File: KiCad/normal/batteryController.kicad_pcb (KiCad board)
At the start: 2 copper layers, 52.5 x 35 mm, 20 parts, among them J1 Screw_Terminal_01x02, J2 Conn_01x04_Male, J3 Conn_01x04_Male, J4 Conn_01x04_Male, J5 Conn_02x04_Odd_Even, J6 Conn_01x01_Male, J7 USB_A, U1 ATtiny45V-10P, U2 LM2596S-ADJ, U3 LP2950-3.3_TO92

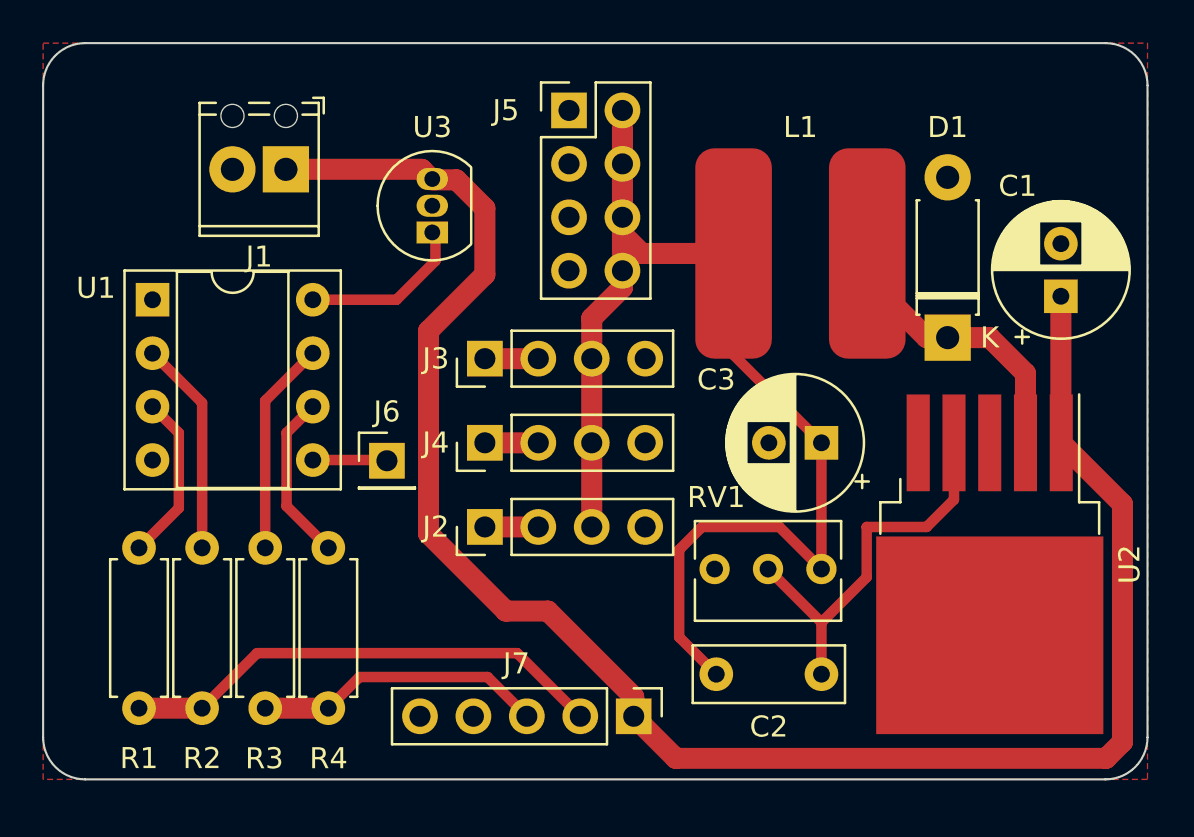
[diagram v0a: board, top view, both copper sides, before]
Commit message: made version using smt components
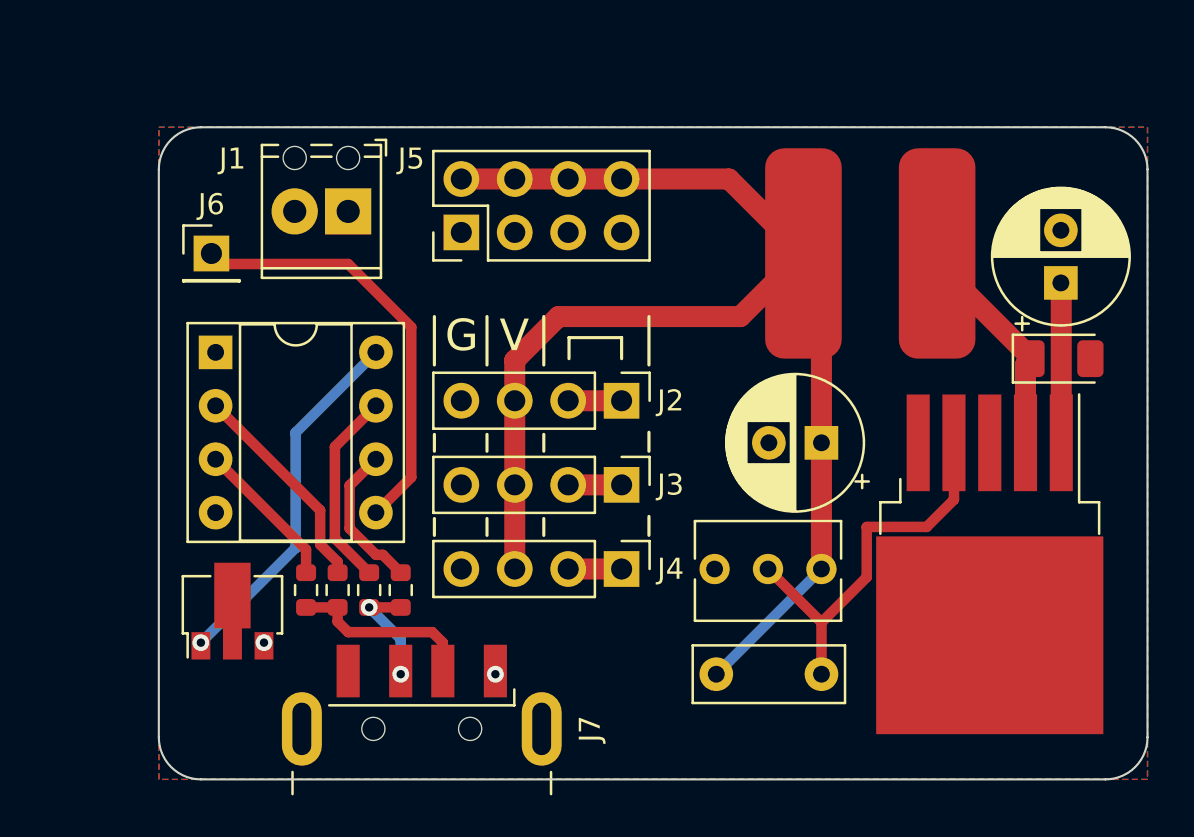
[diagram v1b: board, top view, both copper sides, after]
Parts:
- D1: footprint Diode_THT:D_DO-41_SOD81_P7.62mm_Horizontal -> Diode_SMD:D_1206_3216Metric
- J7: footprint Connector_PinHeader_2.54mm:PinHeader_1x05_P2.54mm_Vertical -> Connector_USB:USB_A_CNCTech_1001-011-01101_Horizontal
- R1, R2, R3, R4: footprint Resistor_THT:R_Axial_DIN0207_L6.3mm_D2.5mm_P7.62mm_Horizontal -> Resistor_SMD:R_0603_1608Metric
- U3: footprint Package_TO_SOT_THT:TO-92_Inline -> Package_TO_SOT_SMD:SOT-89-3
- moved U3 20.4 mm to (57.0, 78.0)
- moved J6 12.9 mm to (56.0, 61.0)
- moved J7 12.6 mm to (66.0, 90.5)
- moved J2 8.85 mm to (75.5, 68.0), turned to -90 degrees
- moved J3 8.85 mm to (75.5, 72.0), turned to -90 degrees
- moved J4 8.85 mm to (75.5, 76.0), turned to -90 degrees
- moved R1 8.19 mm to (60.5, 77.0)
- moved J5 7.74 mm to (67.9, 60.0), turned to 90 degrees
- moved R2 6.75 mm to (62.0, 77.0)
- moved D1 5.48 mm to (96.4, 66.0), turned to 0 degrees
- moved R3 5.33 mm to (63.5, 77.0)
- moved R4 3.98 mm to (65.0, 77.0)
- moved U1 3.91 mm to (56.2, 65.7)
- moved J1 3.57 mm to (62.5, 59.0)
- moved L1 3.32 mm to (87.3, 61.0)
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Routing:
- net /VBUS: track 86.6 -> 7.63 mm, vias 0 -> 2
- net /controll pin: track 3.49 -> 20.5 mm
- net Net-(J7-Pad2): track 23.3 -> 8.94 mm
- net /5V: track 7.45 -> 17.2 mm, vias 0 -> 1
- net /OUT: track 56.7 -> 65.9 mm
- net Net-(J7-Pad3): track 13.8 -> 5.30 mm, vias 0 -> 2
- net /ROUT: track 14.7 -> 11.0 mm
- net Net-(R4-Pad1): track 8.06 -> 7.11 mm
- net Net-(R1-Pad1): track 8.02 -> 7.18 mm
- net Net-(R3-Pad1): track 10.2 -> 9.42 mm
- added copper zone on B.Cu, net /VBUS
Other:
- board size 52.5 x 35 mm -> 47 x 31 mm
- board text added: "G"
- board text added: "V"
